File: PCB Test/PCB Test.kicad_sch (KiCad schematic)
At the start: 1 part, among them U1 ATmega4808-X

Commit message: Started on the PCB design
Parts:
- removed U1: ATmega4808-X, Package_SO:SSOP-28_5.3x10.2mm_P0.65mm, symbol MCU_Microchip_ATmega:ATmega4808-X
- added C1, C2: 100n, symbol Device:C
- added C3: 22n, symbol Device:C
- added R1: 10k, symbol Device:R
- added U1: ATmega4808-A, Package_QFP:TQFP-32_7x7mm_P0.8mm, symbol MCU_Microchip_ATmega:ATmega4808-A
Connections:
- new net +3.3V: C1.1, R1.2, U1.28 (VDD)
- new net +3.3VA: C2.1, U1.18 (AVDD)
- new net DTR: C3.1
- new net GND: C1.2, C2.2, U1.19 (GND), U1.29 (GND)
- new net RESET: C3.2, R1.1, U1.26 (PF6/~{RESET})

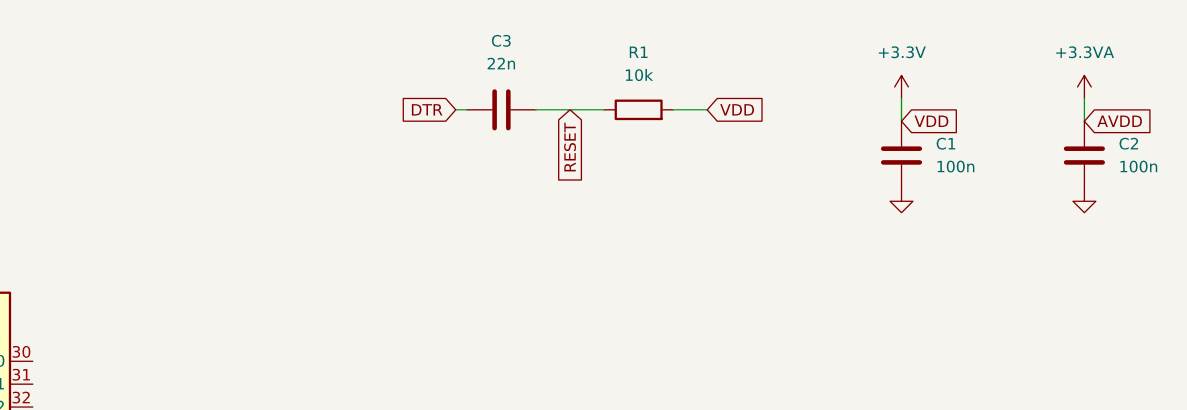
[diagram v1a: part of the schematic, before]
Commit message: Added ground, reset, VDD, AVDD
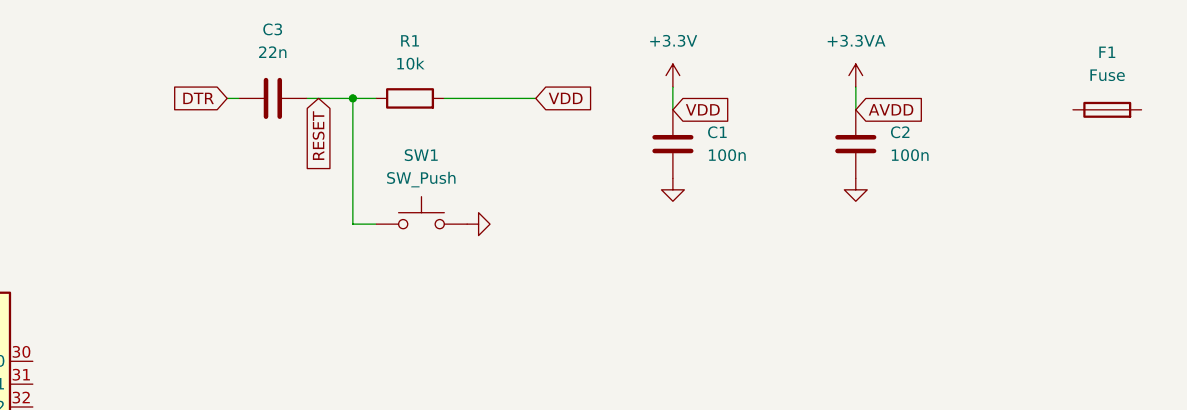
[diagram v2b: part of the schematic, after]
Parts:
- added F1: Fuse, symbol Device:Fuse
- added SW1: SW_Push, symbol Switch:SW_Push
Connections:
- net GND: now also SW1.2
- net RESET: now also SW1.1
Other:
- moved on the sheet: C1, C2, C3, R1

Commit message: Sensors added
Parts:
- removed F1: Fuse, symbol Device:Fuse
- added R2, R3: R, symbol Device:R
- added U2: TCRT5000, tcrt5000:tcrt5000, symbol tcrt5000:TCRT5000
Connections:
- net +3.3V: now also R2.1, U2.COLL
- net GND: now also R3.2, U2.CATH
- new net: R2.2, U2.A
- new net ADC Sensor 1: R3.1, U2.E
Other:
- moved on the sheet: U1

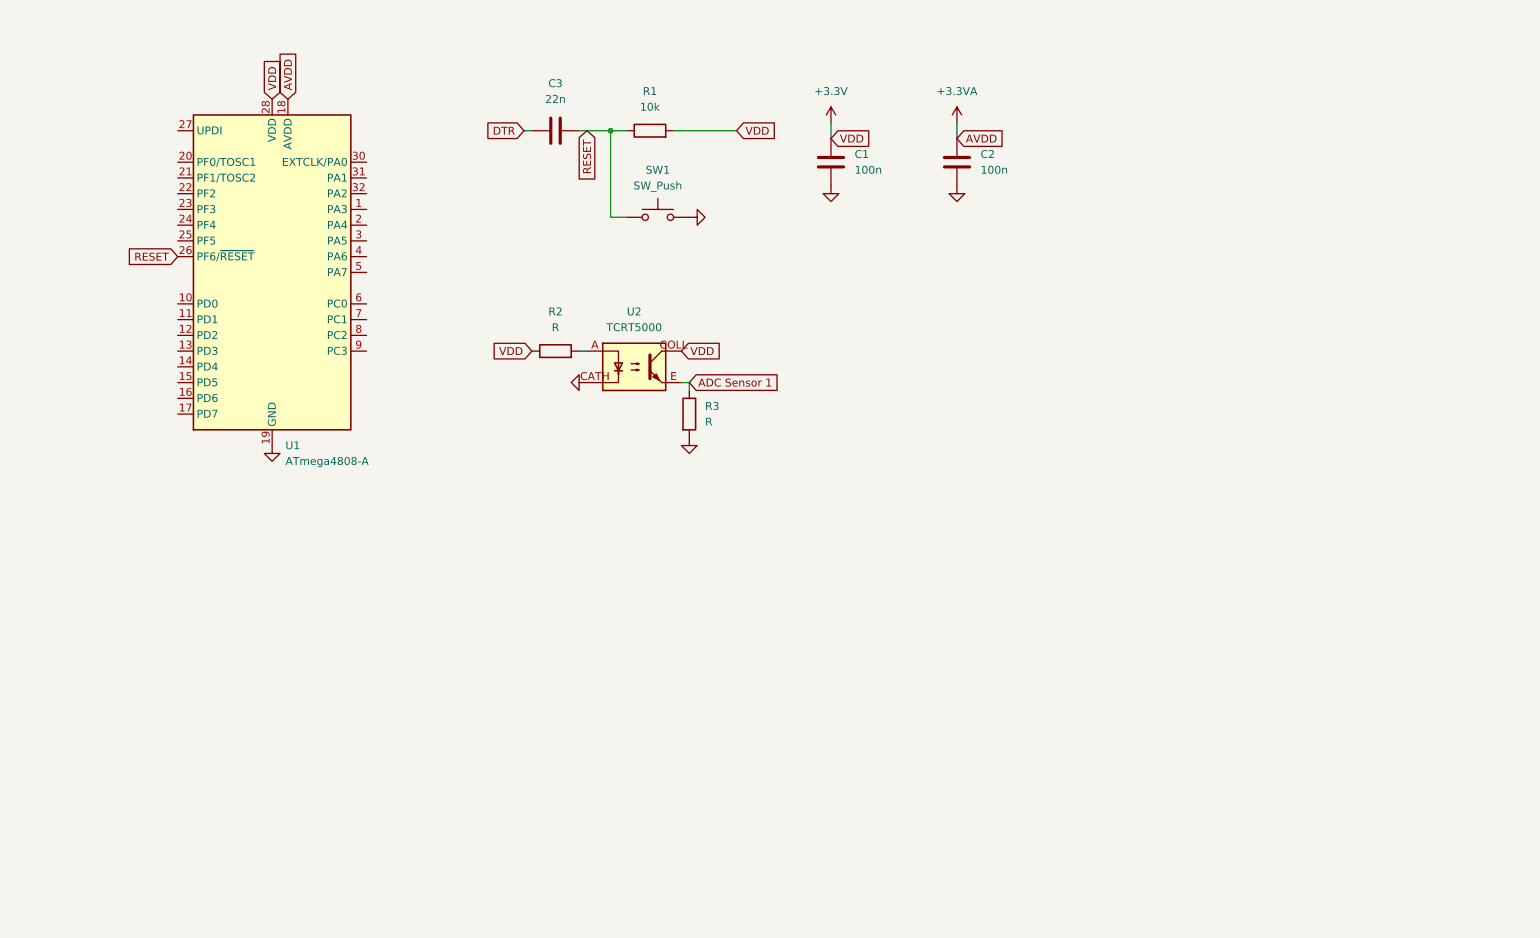
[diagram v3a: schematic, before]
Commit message: Added motors, voltage regulators, sections
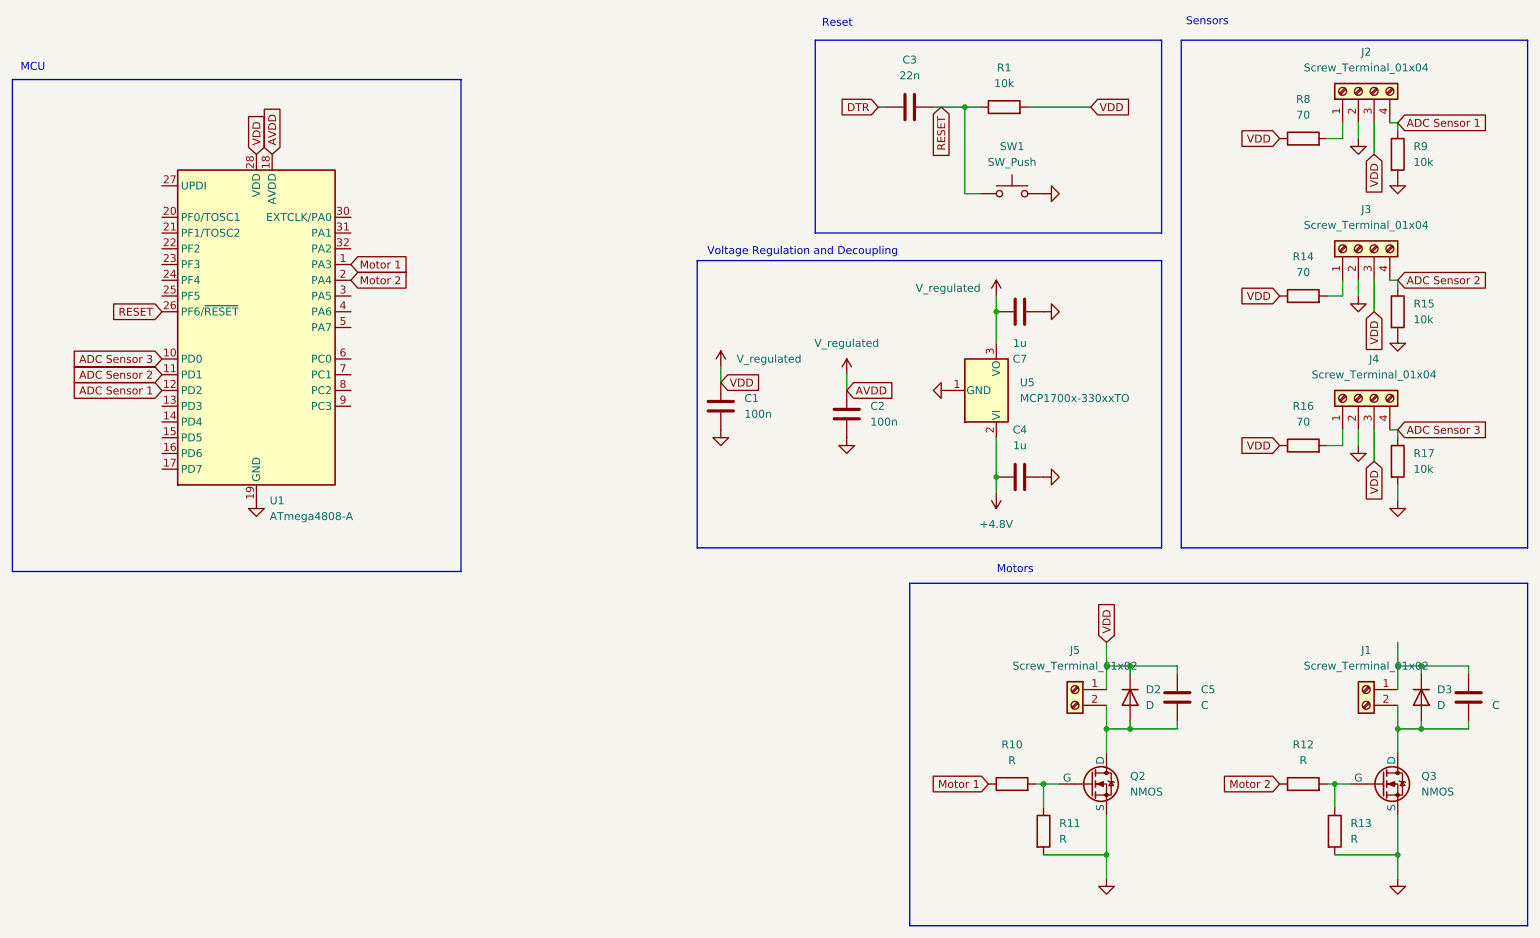
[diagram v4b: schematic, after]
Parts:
- removed R2, R3: R, symbol Device:R
- removed U2: TCRT5000, tcrt5000:tcrt5000, symbol tcrt5000:TCRT5000
- added C4, C7: 1u, symbol Device:C
- added C5, C6: C, symbol Device:C
- added D2, D3: D, symbol Device:D
- added J1, J5: Screw_Terminal_01x02, symbol Connector:Screw_Terminal_01x02
- added J2, J3, J4: Screw_Terminal_01x04, symbol Connector:Screw_Terminal_01x04
- added Q2, Q3: NMOS, symbol Simulation_SPICE:NMOS
- added R10, R11, R12, R13: R, symbol Device:R
- added R14, R16, R8: 70, symbol Device:R
- added R15, R17, R9: 10k, symbol Device:R
- added U5: MCP1700x-330xxTO, Package_TO_SOT_THT:TO-92_Inline, symbol Regulator_Linear:MCP1700x-330xxTO
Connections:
- net +3.3VA is gone; now on net V_regulated: C2.1, U1.18 (AVDD)
- net ADC Sensor 1: now also U1.12 (PD2), J2.4 (Pin_4), R9.1
- net GND: now also C4.2, C7.2, J2.2 (Pin_2), J3.2 (Pin_2), J4.2 (Pin_2), Q2.3 (S), Q3.3 (S), R11.2, R13.2, R15.2, R17.2, R9.2, U5.1 (GND)
- net Motor 1: now reaches U1.1 (PA3)
- net Motor 1: now also R10.1
- net ADC Sensor 3: now reaches U1.10 (PD0)
- net ADC Sensor 3: now also J4.4 (Pin_4), R17.1
- net ADC Sensor 2: now reaches U1.11 (PD1)
- net ADC Sensor 2: now also J3.4 (Pin_4), R15.1
- net Motor 2: now reaches U1.2 (PA4)
- net Motor 2: now also R12.1
- net +3.3V renamed V_regulated
- net V_regulated: now also C5.1, C7.1, D2.1 (K), J2.3 (Pin_3), J3.3 (Pin_3), J4.3 (Pin_3), J5.1 (Pin_1), R14.1, R16.1, R8.1, U5.3 (VO)
- new net: C6.1, D3.1 (K), J1.1 (Pin_1)
- new net: C6.2, D3.2 (A), J1.2 (Pin_2), Q3.1 (D)
- new net: C5.2, D2.2 (A), J5.2 (Pin_2), Q2.1 (D)
- new net: J2.1 (Pin_1), R8.2
- new net: Q3.2 (G), R12.2, R13.1
- new net: J3.1 (Pin_1), R14.2
- new net: Q2.2 (G), R10.2, R11.1
- new net: J4.1 (Pin_1), R16.2
- new net +4.8V: C4.1, U5.2 (VI)
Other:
- note added: "MCU"
- note added: "Motors"
- note added: "Reset"
- note added: "Sensors"
- note added: "Voltage Regulation and Decoupling"
- moved on the sheet: C1, C2, C3, R1, SW1, U1

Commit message: Added ENEL270 Arduino
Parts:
- added J6: Conn_02x03_Odd_Even, symbol Connector_Generic:Conn_02x03_Odd_Even
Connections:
- net GND: now also J6.6 (Pin_6)
- net RESET: now also J6.5 (Pin_5)
- net V_regulated: now also J6.2 (Pin_2)
- net UPDI Data: now reaches U1.27 (UPDI)
- net UPDI Data: now also J6.1 (Pin_1)
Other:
- note added: "ENEL270 Connector"

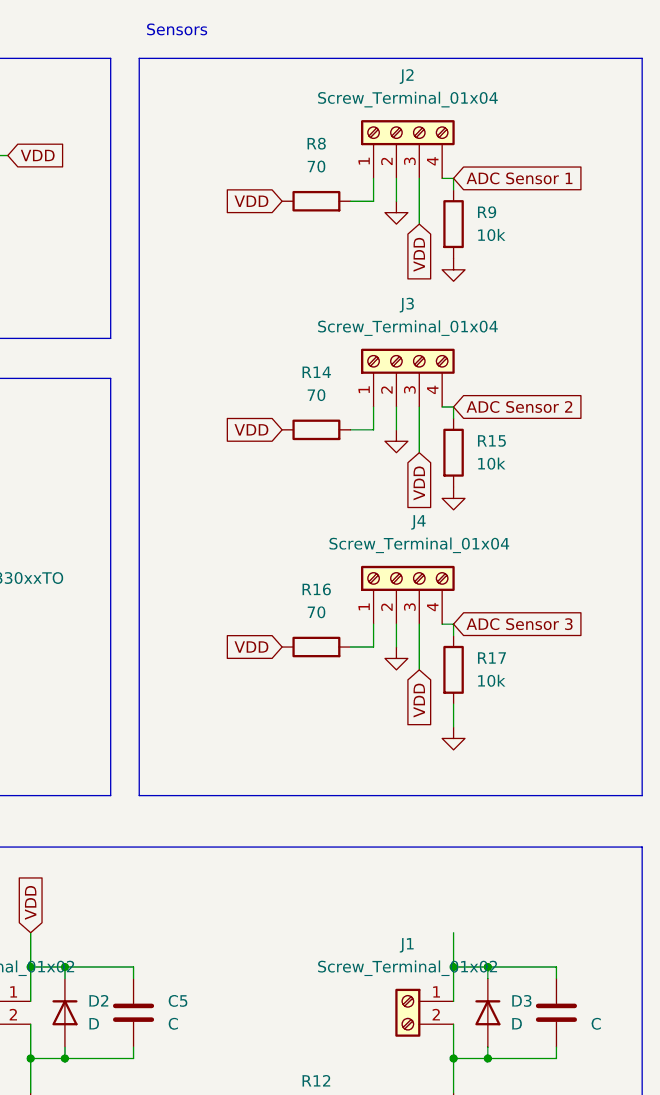
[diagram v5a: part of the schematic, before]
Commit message: Switched pins for sensors
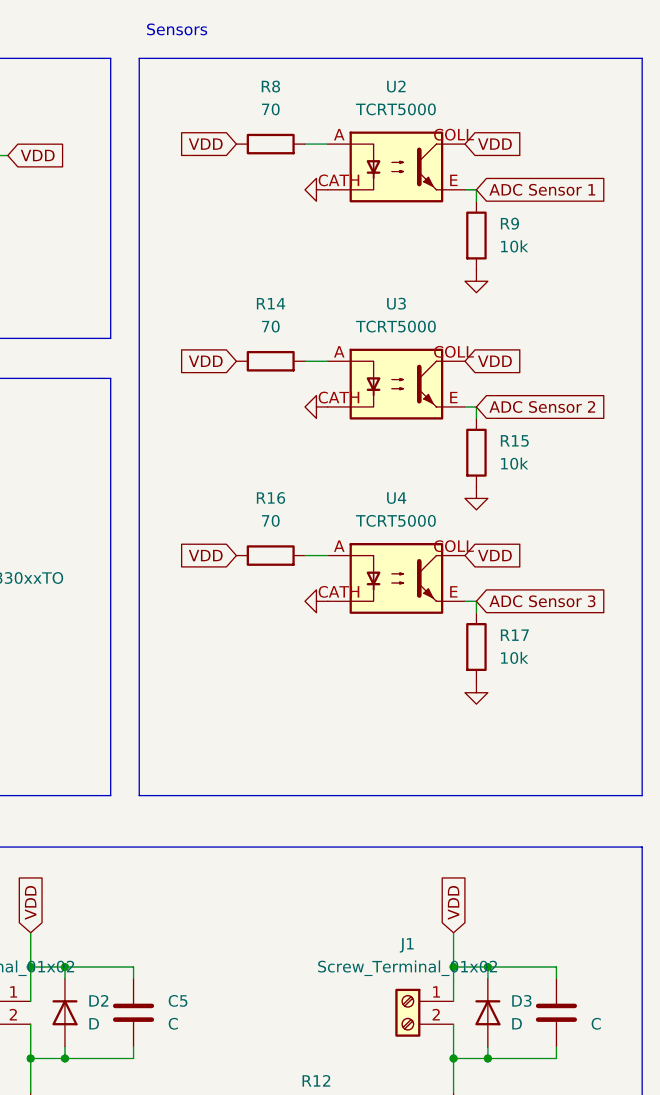
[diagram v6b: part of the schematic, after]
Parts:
- removed J2, J3, J4: Screw_Terminal_01x04, symbol Connector:Screw_Terminal_01x04
- added U2, U3, U4: TCRT5000, tcrt5000:tcrt5000, symbol tcrt5000:TCRT5000
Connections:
- net ADC Sensor 1: now also U2.E
- net ADC Sensor 2: now also U3.E
- net ADC Sensor 3: now also U4.E
- net GND: now also U2.CATH, U3.CATH, U4.CATH
- net V_regulated: now also C6.1, D3.1 (K), J1.1 (Pin_1), U2.COLL, U3.COLL, U4.COLL
- net at R8.2: now also U2.A
- net at R14.2: now also U3.A
- net at R16.2: now also U4.A
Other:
- moved on the sheet: R8, R9
